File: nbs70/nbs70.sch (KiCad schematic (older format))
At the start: 110 parts

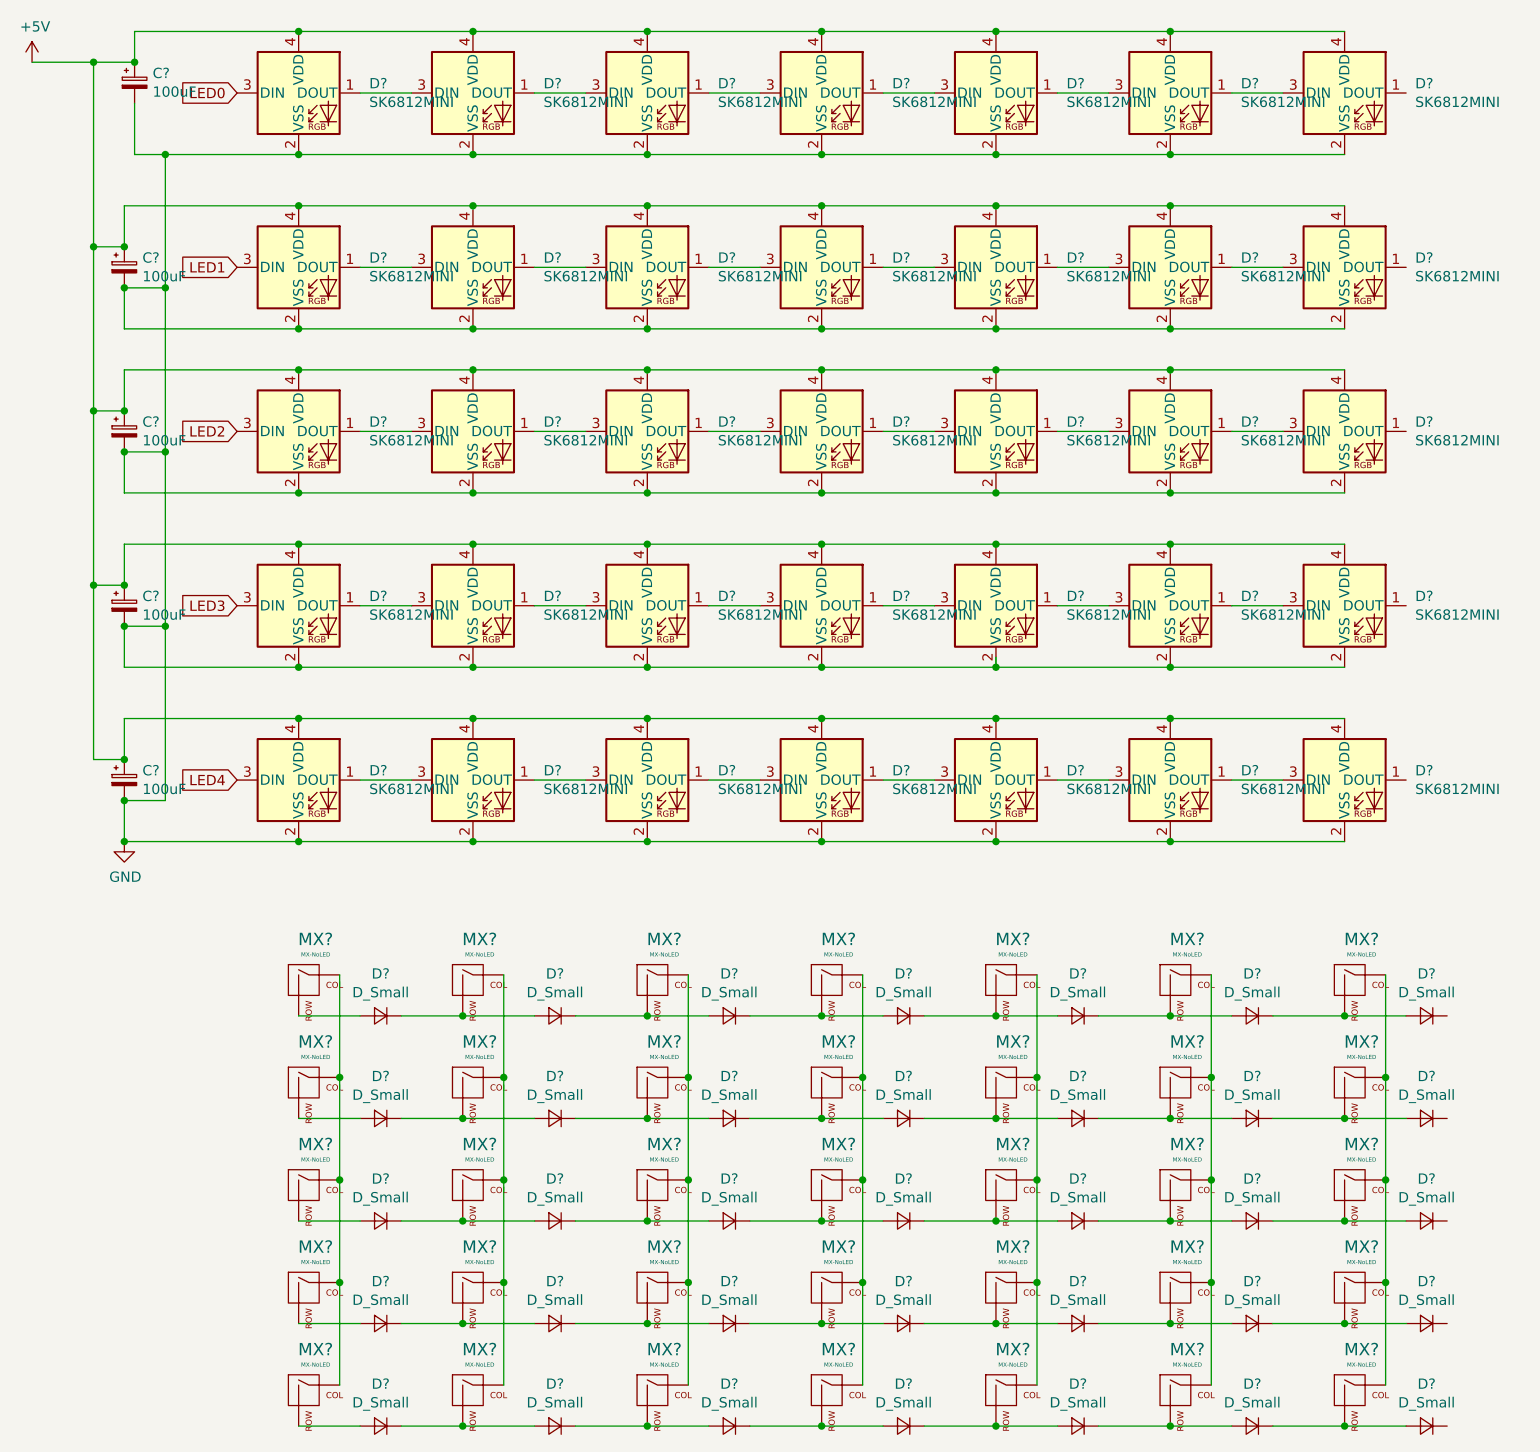
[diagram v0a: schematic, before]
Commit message: LEDs and switch matrix
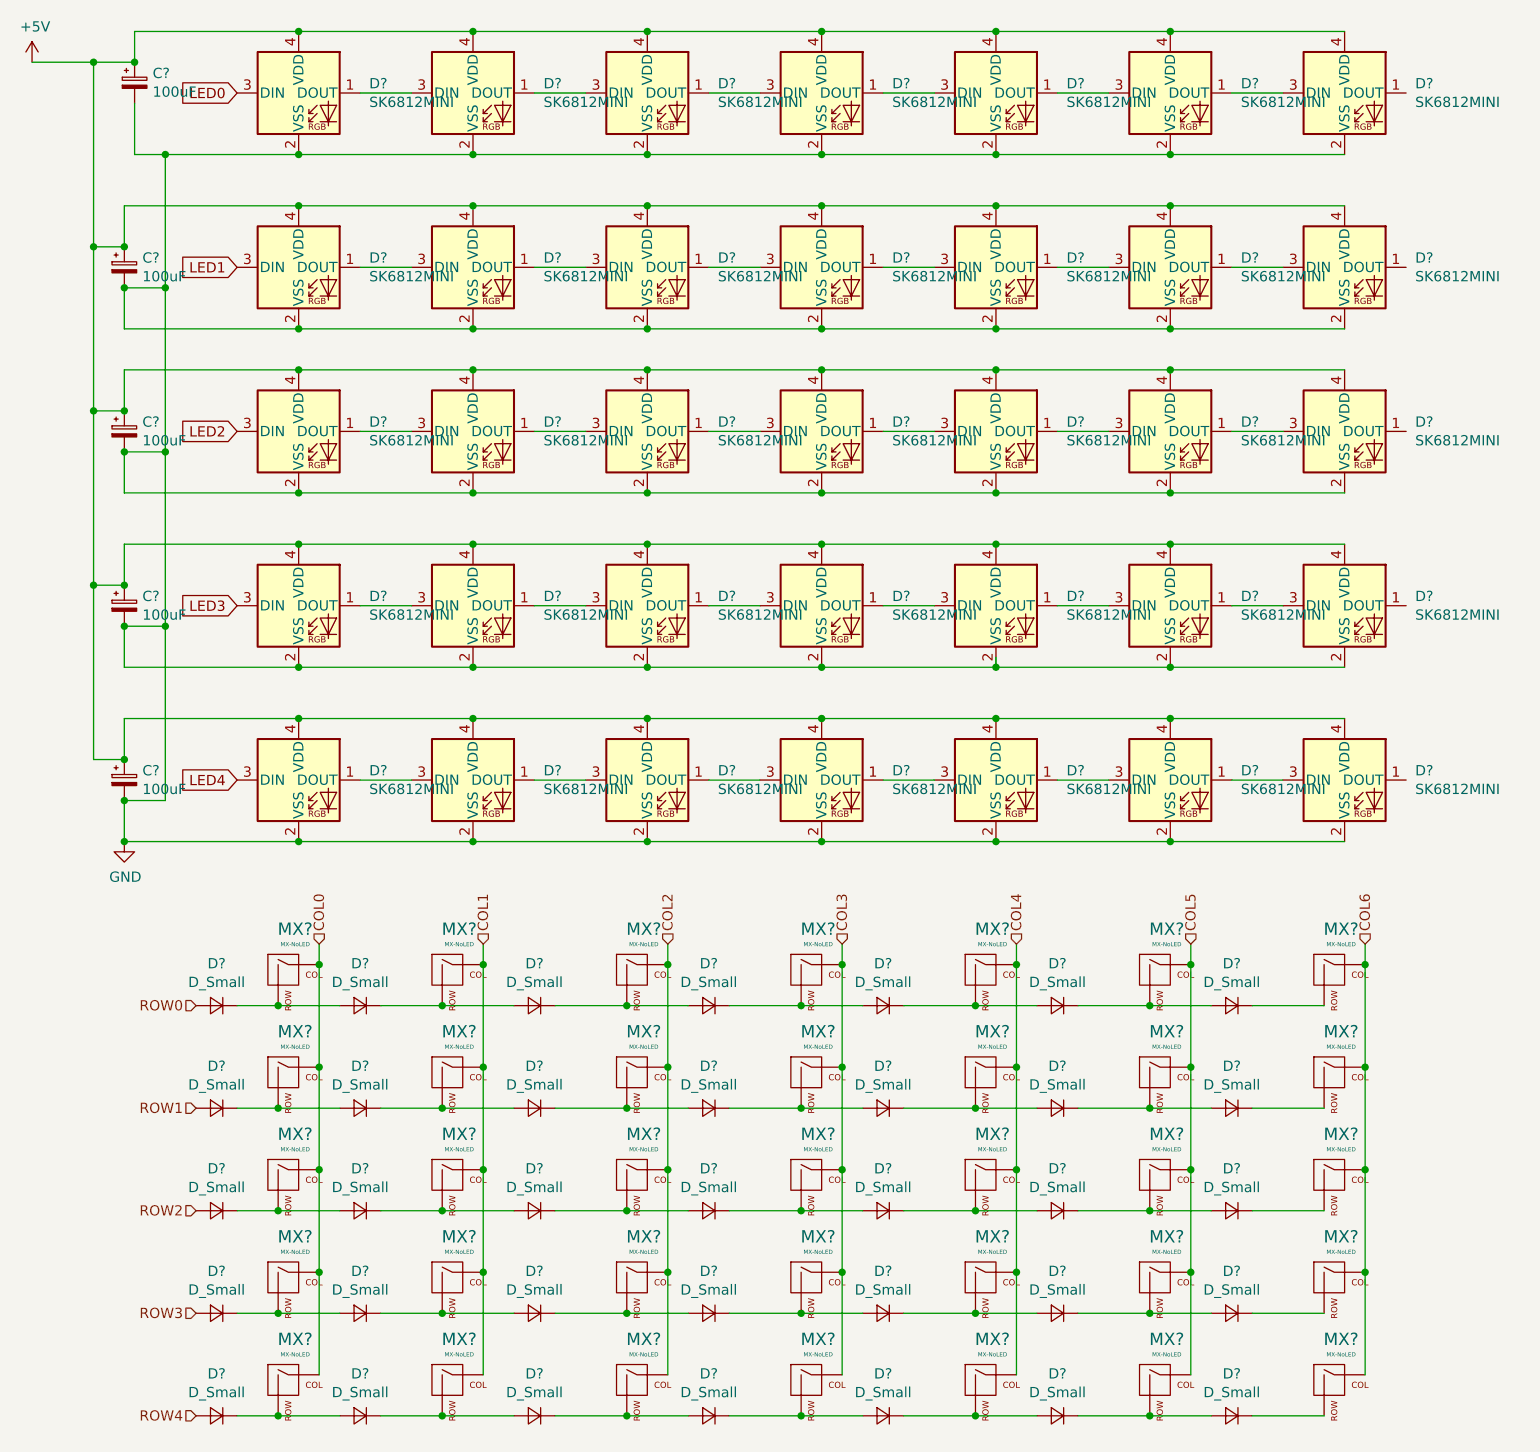
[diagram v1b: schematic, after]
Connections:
- net COL0: now reaches MX?.1 (COL), MX?.1 (COL), MX?.1 (COL), MX?.1 (COL), MX?.1 (COL)
- net at D?.2 (A), MX?.2 (ROW): now also D?.1 (K) (x5)
- net COL1: now reaches MX?.1 (COL), MX?.1 (COL), MX?.1 (COL), MX?.1 (COL), MX?.1 (COL)
- net COL2: now reaches MX?.1 (COL), MX?.1 (COL), MX?.1 (COL), MX?.1 (COL), MX?.1 (COL)
- net COL3: now reaches MX?.1 (COL), MX?.1 (COL), MX?.1 (COL), MX?.1 (COL), MX?.1 (COL)
- net COL4: now reaches MX?.1 (COL), MX?.1 (COL), MX?.1 (COL), MX?.1 (COL), MX?.1 (COL)
- net COL5: now reaches MX?.1 (COL), MX?.1 (COL), MX?.1 (COL), MX?.1 (COL), MX?.1 (COL)
- net COL6: now reaches MX?.1 (COL), MX?.1 (COL), MX?.1 (COL), MX?.1 (COL), MX?.1 (COL)
- net at D?.1 (K), MX?.2 (ROW): no longer D?.2 (A) (x5)
- new net ROW0: D?.2 (A)
- new net ROW1: D?.2 (A)
- new net ROW2: D?.2 (A)
- new net ROW3: D?.2 (A)
- new net ROW4: D?.2 (A)
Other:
- moved on the sheet: D?, MX?
